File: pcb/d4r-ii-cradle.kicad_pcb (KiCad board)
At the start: 2 copper layers, 36 x 36 mm, 23 parts, among them P1 CONN_02X06, P2 CONN_01X04, P3 CONN_01X02, Q1 Q_NMOS_GSD, Q2 Q_NMOS_GSD

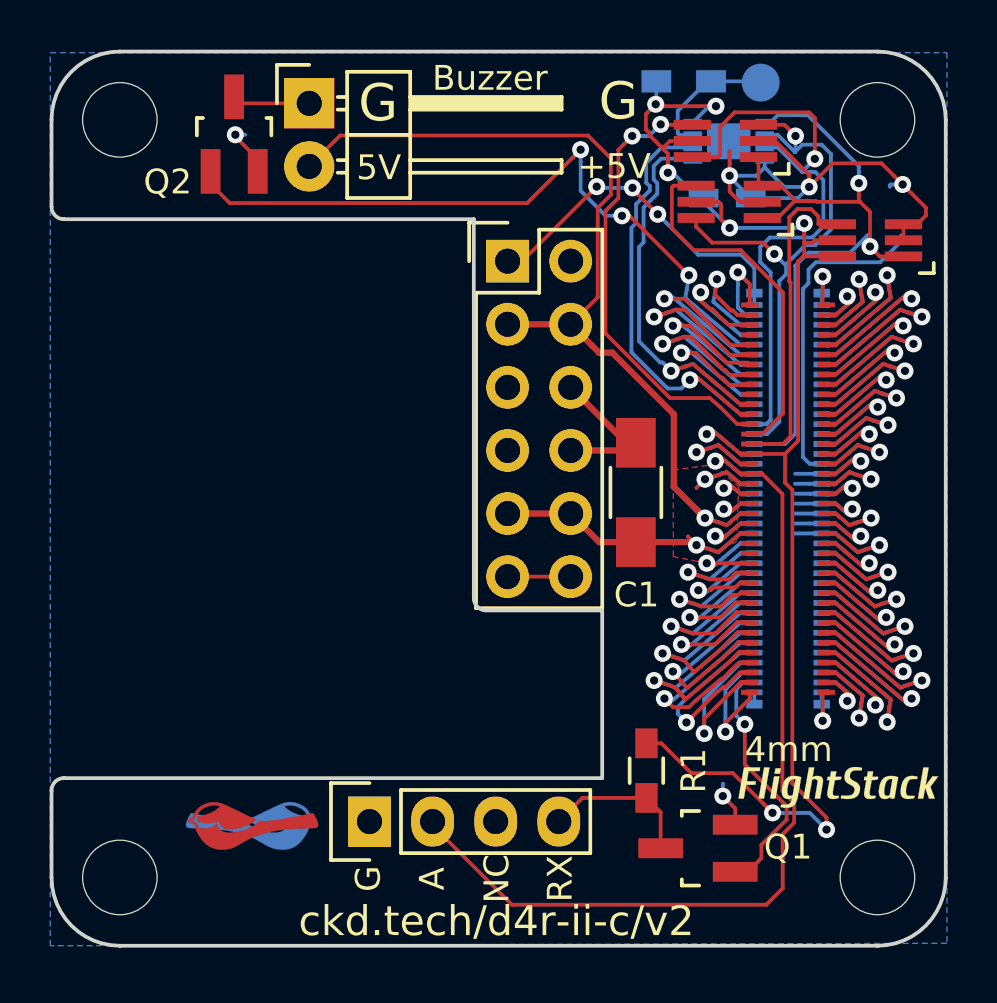
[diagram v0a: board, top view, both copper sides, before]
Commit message: Rebrand everything to Polystack and increment versions.
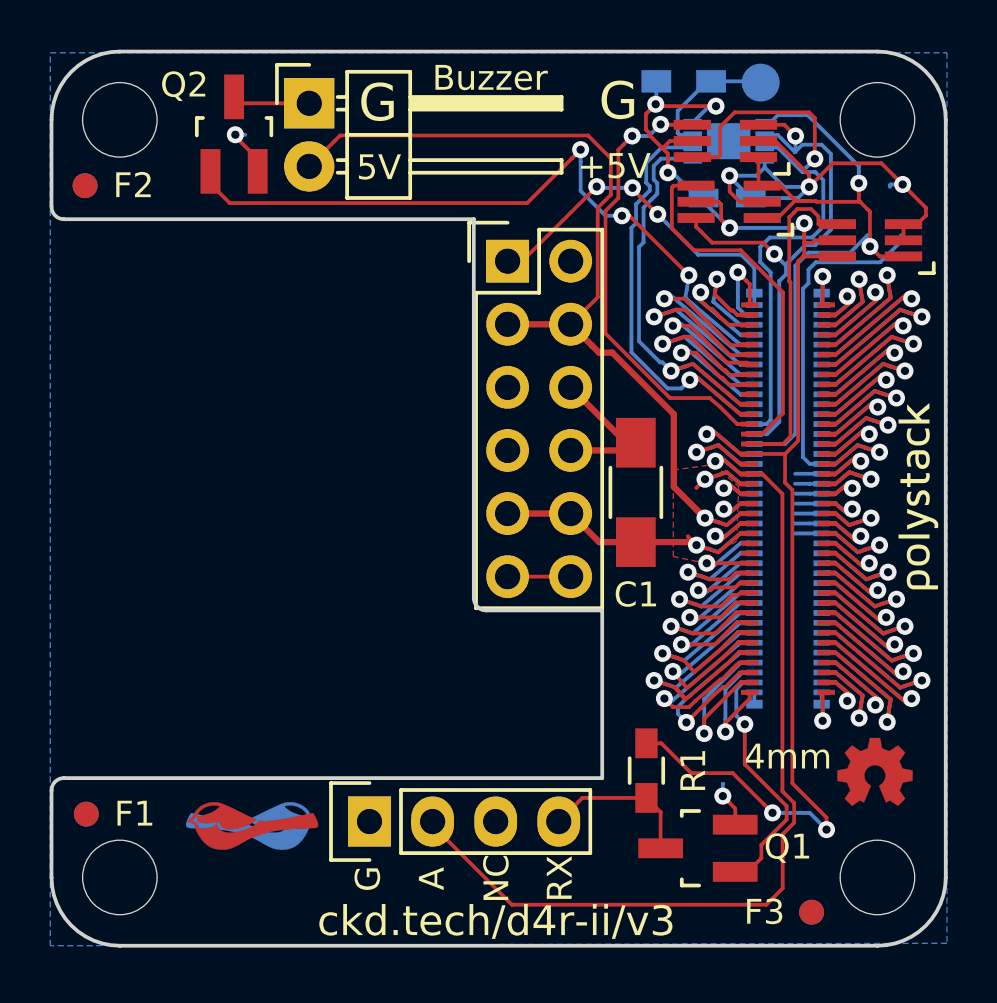
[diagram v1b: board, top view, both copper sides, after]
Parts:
- removed the G*** at (161.7, 119.6)
- added F1: 1mm, macrofab:Fiducial, F.Cu at (131.4, 120.7)
- added F2: 1mm, macrofab:Fiducial, F.Cu at (131.3, 95.4)
- added F3: 1mm, macrofab:Fiducial, F.Cu at (160.6, 124.7)
- added F4: 1mm, macrofab:Fiducial, B.Cu at (131.4, 120.7)
- added F5: 1mm, macrofab:Fiducial, B.Cu at (131.3, 95.4)
- added F6: 1mm, macrofab:Fiducial, B.Cu at (160.6, 124.7)
- added G***: OSHW, oshw:oshw-3mm, F.Cu at (163.2, 119.0)
- added svg2mod: G***, polystack:polystack-medium-0.4, B.Cu at (164.9, 107.9)
- added svg2mod: G***, polystack:polystack-medium-0.4, F.Cu at (164.9, 107.9)
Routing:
- net GNDPWR: track 83.6 -> 82.6 mm
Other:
- rule pad_to_mask_clearance: 0.2 -> 0.0762
- board text added: "ckd.tech/d4r-ii/v3"
- board text removed: "ckd.tech/d4r-ii-c/v2"
